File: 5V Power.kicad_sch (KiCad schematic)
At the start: 1 part, among them U3 TPS54540BDDA

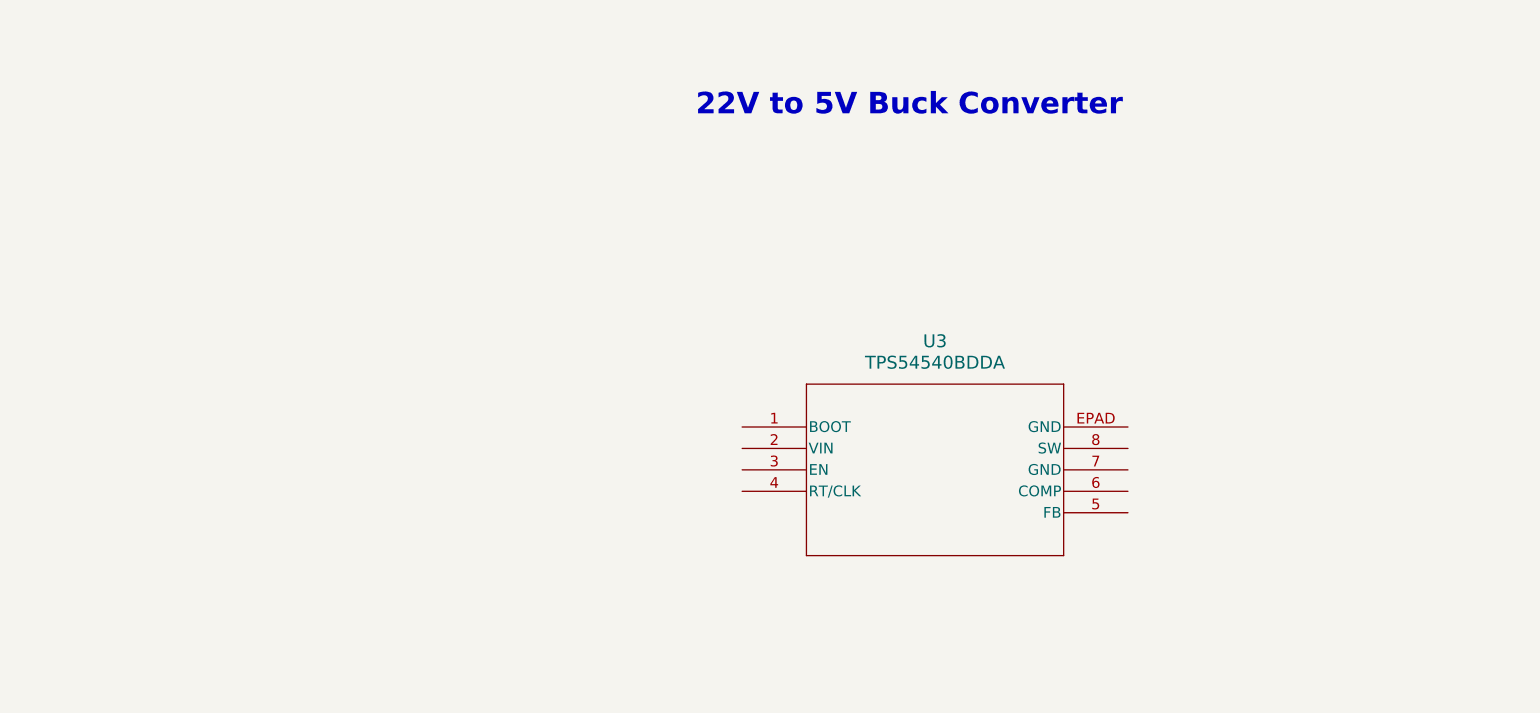
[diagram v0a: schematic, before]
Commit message: Updates to the 5V buck converter
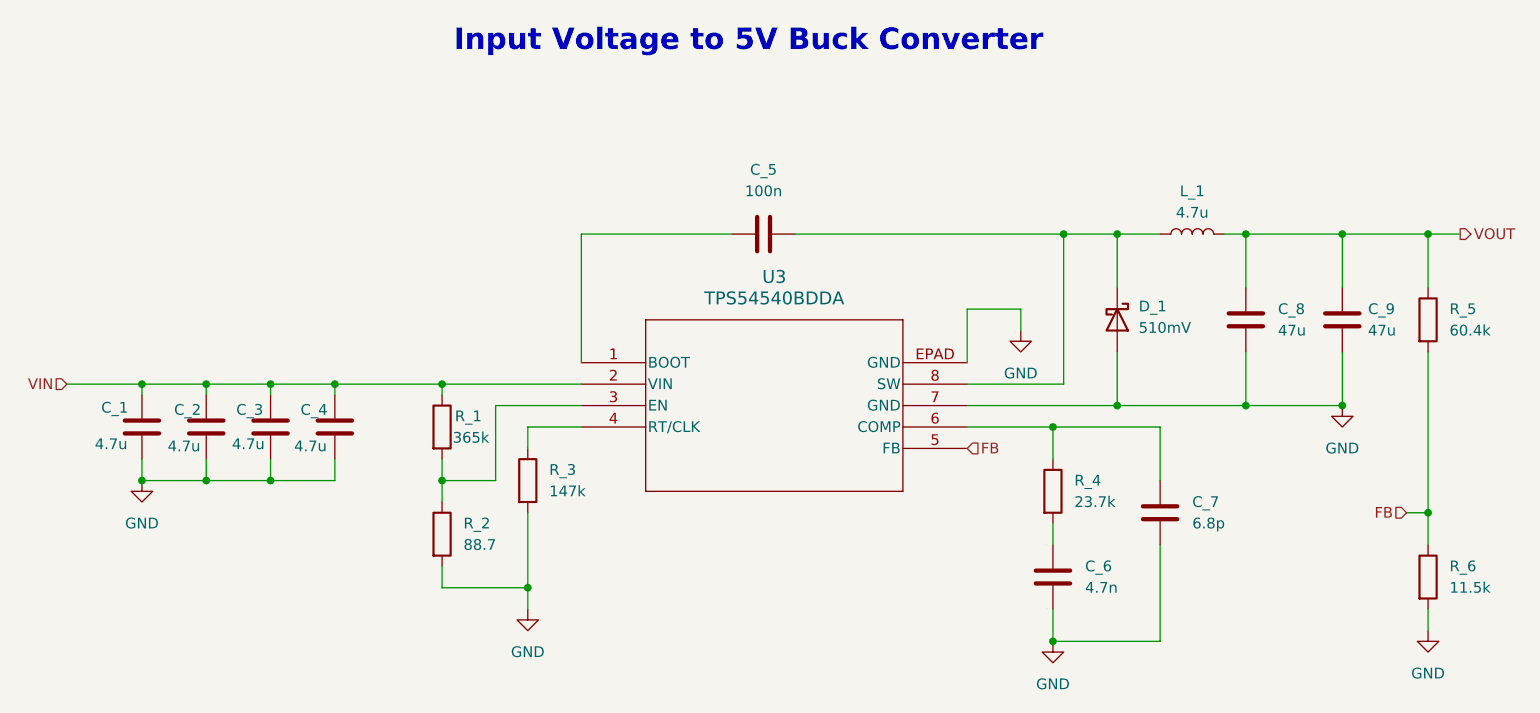
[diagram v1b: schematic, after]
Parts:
- added C_1, C_2, C_3, C_4: 4.7u, symbol Device:C
- added C_5: 100n, symbol Device:C
- added C_6: 4.7n, symbol Device:C
- added C_7: 6.8p, symbol Device:C
- added C_8, C_9: 47u, symbol Device:C
- added D_1: 510mV, symbol Device:D_Schottky
- added L_1: 4.7u, symbol Device:L
- added R_1: 365k, symbol Device:R
- added R_2: 88.7, symbol Device:R
- added R_3: 147k, symbol Device:R
- added R_4: 23.7k, symbol Device:R
- added R_5: 60.4k, symbol Device:R
- added R_6: 11.5k, symbol Device:R
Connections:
- net at U3.1 (BOOT): now also C_5.2
- net VIN: now reaches U3.2 (VIN)
- net VIN: now also C_1.1, C_2.1, C_3.1, C_4.1, R_1.1
- net at U3.3 (EN): now also R_1.2, R_2.1
- net at U3.4 (RT/CLK): now also R_3.1
- net FB: now reaches U3.5 (FB)
- net FB: now also R_5.2, R_6.1
- net at U3.6 (COMP): now also C_7.1, R_4.1
- net GND: now reaches U3.7 (GND)
- net GND: now also U3.EPAD (GND), C_1.2, C_2.2, C_3.2, C_4.2, C_6.2, C_7.2, C_8.2, C_9.2, D_1.2 (A), R_2.2, R_3.2, R_6.2
- net at U3.8 (SW): now also C_5.1, D_1.1 (K), L_1.1
- new net: C_6.1, R_4.2
- new net VOUT: C_8.1, C_9.1, L_1.2, R_5.1
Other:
- note added: "Input Voltage to 5V Buck Converter"
- note removed: "22V to 5V Buck Converter"
- moved on the sheet: U3

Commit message: Added new potentiometer
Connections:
- net VOUT renamed +5V
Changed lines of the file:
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@@
-		)
-	)
-	(hierarchical_label "VOUT"
-		(shape output)
-		(at 203.2 72.39 0)
-		(effects
-			(font
-				(size 1.27 1.27)
-			)
-			(justify left)
 		)
 	)
@@
 		)
 	)
+	(symbol
+		(lib_id "power:+5V")
+		(at 203.2 72.39 0)
+		(unit 1)
+		(body_style 1)
+		(exclude_from_sim no)
+		(in_bom yes)
+		(on_board yes)
+		(in_pos_files yes)
+		(dnp no)
+		(fields_autoplaced yes)
+		(property "Reference" "#PWR022"
+			(at 203.2 76.2 0)
+			(hide yes)
+			(show_name no)
+			(do_not_autoplace no)
+			(effects
+				(font
+					(size 1.27 1.27)
+				)
+			)
+		)
+		(property "Value" "+5V"
+			(at 203.2 67.31 0)
+			(show_name no)
+			(do_not_autoplace no)
+			(effects
+				(font
+					(size 1.27 1.27)
+				)
+			)
+		)
+		(property "Footprint" ""
+			(at 203.2 72.39 0)
+			(hide yes)
+			(show_name no)
+			(do_not_autoplace no)
+			(effects
+				(font
+					(size 1.27 1.27)
+				)
+			)
+		)
+		(property "Datasheet" ""
+			(at 203.2 72.39 0)
+			(hide yes)
+			(show_name no)
+			(do_not_autoplace no)
+			(effects
+				(font
+					(size 1.27 1.27)
+				)
+			)
+		)
+		(property "Description" "Power symbol creates a global label with name \"+5V\""
+			(at 203.2 72.39 0)
+			(hide yes)
+			(show_name no)
+			(do_not_autoplace no)
+			(effects
+				(font
+					(size 1.27 1.27)
+				)
+			)
+		)
+		(pin "1"
+		)
+		(instances
+			(project "LEOS-F26-power"
+				(path "/3703ddf2-8141-438d-86a8-1eaec9672d0d/528ff9b0-a904-4a78-86c6-11cbf84face6"
+					(reference "#PWR022")
+					(unit 1)
+				)
+			)
+		)
+	)

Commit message: added footprints
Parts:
- C_1, C_2, C_3, C_4, C_5, C_6, C_7, C_8, C_9: footprint (none) -> Capacitor_SMD:C_0805_2012Metric
- D_1: footprint (none) -> Diode_SMD:D_0805_2012Metric
- L_1: footprint (none) -> Inductor_SMD:L_0805_2012Metric
- R_1, R_2, R_3, R_4, R_5, R_6: footprint (none) -> Resistor_SMD:R_0805_2012Metric
- U3: footprint SO-POWERPAD8_DDA_TEX -> (none)
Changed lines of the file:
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@@
 			)
 		)
-		(property "Footprint" ""
+		(property "Footprint" "Capacitor_SMD:C_0805_2012Metric"
 			(at 63.1952 99.06 0)
 			(hide yes)
@@
 			)
 		)
-		(property "Footprint" ""
+		(property "Footprint" "Capacitor_SMD:C_0805_2012Metric"
 			(at 47.9552 99.06 0)
 			(hide yes)
@@
 			)
 		)
-		(property "Footprint" ""
+		(property "Footprint" "Capacitor_SMD:C_0805_2012Metric"
 			(at 178.7652 86.36 0)
 			(hide yes)
@@
 			)
 		)
-		(property "Footprint" "SO-POWERPAD8_DDA_TEX"
+		(property "Footprint" ""
 			(at 99.06 87.63 0)
 			(hide yes)
@@
 			)
 		)
-		(property "Footprint" ""
+		(property "Footprint" "Resistor_SMD:R_0805_2012Metric"
 			(at 197.612 82.55 90)
 			(hide yes)
@@
 			)
 		)
-		(property "Footprint" ""
+		(property "Footprint" "Resistor_SMD:R_0805_2012Metric"
 			(at 80.772 95.25 90)
 			(hide yes)
@@
 			)
 		)
-		(property "Footprint" ""
+		(property "Footprint" "Resistor_SMD:R_0805_2012Metric"
 			(at 90.932 101.6 90)
 			(hide yes)
@@
 			)
 		)
-		(property "Footprint" ""
+		(property "Footprint" "Inductor_SMD:L_0805_2012Metric"
 			(at 171.45 72.39 0)
 			(hide yes)
@@
 			)
 		)
-		(property "Footprint" ""
+		(property "Footprint" "Capacitor_SMD:C_0805_2012Metric"
 			(at 190.1952 86.36 0)
 			(hide yes)
@@
 			)
 		)
-		(property "Footprint" ""
+		(property "Footprint" "Capacitor_SMD:C_0805_2012Metric"
 			(at 55.5752 99.06 0)
 			(hide yes)
@@
 			)
 		)
-		(property "Footprint" ""
+		(property "Footprint" "Capacitor_SMD:C_0805_2012Metric"
 			(at 70.8152 99.06 0)
 			(hide yes)
@@
 			)
 		)
-		(property "Footprint" ""
+		(property "Footprint" "Resistor_SMD:R_0805_2012Metric"
 			(at 80.772 107.95 90)
 			(hide yes)
@@
 			)
 		)
-		(property "Footprint" ""
+		(property "Footprint" "Capacitor_SMD:C_0805_2012Metric"
 			(at 168.6052 109.22 0)
 			(hide yes)
@@
 			)
 		)
-		(property "Footprint" ""
+		(property "Footprint" "Resistor_SMD:R_0805_2012Metric"
 			(at 153.162 102.87 90)
 			(hide yes)
@@
 			)
 		)
-		(property "Footprint" ""
+		(property "Footprint" "Resistor_SMD:R_0805_2012Metric"
 			(at 197.612 113.03 90)
 			(hide yes)
@@
 			)
 		)
-		(property "Footprint" ""
+		(property "Footprint" "Diode_SMD:D_0805_2012Metric"
 			(at 162.56 82.55 0)
 			(hide yes)
@@
 			)
 		)
-		(property "Footprint" ""
+		(property "Footprint" "Capacitor_SMD:C_0805_2012Metric"
 			(at 155.9052 116.84 0)
 			(hide yes)
@@
 			)
 		)
-		(property "Footprint" ""
+		(property "Footprint" "Capacitor_SMD:C_0805_2012Metric"
 			(at 116.84 73.3552 0)
 			(hide yes)

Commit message: testing
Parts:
- C_1, C_2, C_3, C_4: Digikey (none) -> 1276-2970-1-ND; MPN (none) -> CL21B475KOFNFNE; Manufacturer (none) -> Samsung Electro-Mechanics
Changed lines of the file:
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@@
+			)
+		)
+		(property "Digikey" "1276-2970-1-ND"
+			(at 62.23 95.25 0)
+			(hide yes)
+			(show_name no)
+			(do_not_autoplace no)
+			(effects
+				(font
+					(size 1.27 1.27)
+				)
+			)
+		)
+		(property "MPN" "CL21B475KOFNFNE"
+			(at 62.23 95.25 0)
+			(hide yes)
+			(show_name no)
+			(do_not_autoplace no)
+			(effects
+				(font
+					(size 1.27 1.27)
+				)
+			)
+		)
+		(property "Manufacturer" "Samsung Electro-Mechanics"
+			(at 62.23 95.25 0)
+			(hide yes)
+			(show_name no)
+			(do_not_autoplace no)
+			(effects
+				(font
+					(size 1.27 1.27)
+				)
 			)
 		)
@@
 		)
 		(property "Description" "Unpolarized capacitor"
+			(at 46.99 95.25 0)
+			(hide yes)
+			(show_name no)
+			(do_not_autoplace no)
+			(effects
+				(font
+					(size 1.27 1.27)
+				)
+			)
+		)
+		(property "Digikey" "1276-2970-1-ND"
+			(at 46.99 95.25 0)
+			(hide yes)
+			(show_name no)
+			(do_not_autoplace no)
+			(effects
+				(font
+					(size 1.27 1.27)
+				)
+			)
+		)
+		(property "MPN" "CL21B475KOFNFNE"
+			(at 46.99 95.25 0)
+			(hide yes)
+			(show_name no)
+			(do_not_autoplace no)
+			(effects
+				(font
+					(size 1.27 1.27)
+				)
+			)
+		)
+		(property "Manufacturer" "Samsung Electro-Mechanics"
 			(at 46.99 95.25 0)
 			(hide yes)
@@
 			)
 		)
+		(property "Digikey" "1276-2970-1-ND"
+			(at 54.61 95.25 0)
+			(hide yes)
+			(show_name no)
+			(do_not_autoplace no)
+			(effects
+				(font
+					(size 1.27 1.27)
+				)
+			)
+		)
+		(property "MPN" "CL21B475KOFNFNE"
+			(at 54.61 95.25 0)
+			(hide yes)
+			(show_name no)
+			(do_not_autoplace no)
+			(effects
+				(font
+					(size 1.27 1.27)
+				)
+			)
+		)
+		(property "Manufacturer" "Samsung Electro-Mechanics"
+			(at 54.61 95.25 0)
+			(hide yes)
+			(show_name no)
+			(do_not_autoplace no)
+			(effects
+				(font
+					(size 1.27 1.27)
+				)
+			)
+		)
 		(pin "2"
 		)
@@
 			(at 69.85 95.25 0)
 			(hide yes)
+			(show_name no)
+			(do_not_autoplace no)
+			(effects
+				(font
+					(size 1.27 1.27)
+				)
+			)
+		)
+		(property "Digikey" "1276-2970-1-ND"
+			(at 69.85 95.25 0)
+			(hide yes)
+			(show_name no)
+			(do_not_autoplace no)
+			(effects
+				(font
+					(size 1.27 1.27)
+				)
+			)
+		)
+		(property "MPN" "CL21B475KOFNFNE"
+			(at 69.85 95.25 0)
+			(hide yes)
+			(show_name no)
+			(do_not_autoplace no)
+			(effects
+				(font
+					(size 1.27 1.27)
+				)
+			)
+		)
+		(property "Manufacturer" "Samsung Electro-Mechanics"
+			(at 69.85 95.25 0)
+			(hide yes)

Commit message: capacitor
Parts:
- C_6: Digikey (none) -> 399-C0805C472J3GEC7210CT-ND; MPN (none) -> C0805C472J3GEC7210; Manufacturer (none) -> KEMET
- C_7: Digikey (none) -> 399-C0805C689C3HACAUTOCT-ND; MPN (none) -> C0805C689C3HACAUTO; Manufacturer (none) -> KEMET
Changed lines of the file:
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@@
+			)
+		)
+		(property "Digikey" "399-C0805C689C3HACAUTOCT-ND"
+			(at 167.64 105.41 0)
+			(hide yes)
+			(show_name no)
+			(do_not_autoplace no)
+			(effects
+				(font
+					(size 1.27 1.27)
+				)
+			)
+		)
+		(property "MPN" "C0805C689C3HACAUTO"
+			(at 167.64 105.41 0)
+			(hide yes)
+			(show_name no)
+			(do_not_autoplace no)
+			(effects
+				(font
+					(size 1.27 1.27)
+				)
+			)
+		)
+		(property "Manufacturer" "KEMET"
+			(at 167.64 105.41 0)
+			(hide yes)
+			(show_name no)
+			(do_not_autoplace no)
+			(effects
+				(font
+					(size 1.27 1.27)
+				)
 			)
 		)
@@
 			(at 154.94 113.03 0)
 			(hide yes)
+			(show_name no)
+			(do_not_autoplace no)
+			(effects
+				(font
+					(size 1.27 1.27)
+				)
+			)
+		)
+		(property "Digikey" "399-C0805C472J3GEC7210CT-ND"
+			(at 154.94 113.03 0)
+			(hide yes)
+			(show_name no)
+			(do_not_autoplace no)
+			(effects
+				(font
+					(size 1.27 1.27)
+				)
+			)
+		)
+		(property "MPN" "C0805C472J3GEC7210"
+			(at 154.94 113.03 0)
+			(hide yes)
+			(show_name no)
+			(do_not_autoplace no)
+			(effects
+				(font
+					(size 1.27 1.27)
+				)
+			)
+		)
+		(property "Manufacturer" "KEMET"
+			(at 154.94 113.03 0)
+			(hide yes)

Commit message: resistor values
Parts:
- R_1: Digikey (none) -> RMCF0805FT365KCT-ND; MPN (none) -> RMCF0805FT365K; Manufacturer (none) -> Stackpole Electronics Inc
- R_2: Digikey (none) -> 738-RMCF0805FT88R7CT-ND; MPN (none) -> RMCF0805FT88R7; Manufacturer (none) -> Stackpole Electronics Inc
- R_3: Digikey (none) -> RMCF0805FT147KCT-ND; MPN (none) -> RMCF0805FT147K; Manufacturer (none) -> Stackpole Electronics Inc
- R_4: Digikey (none) -> 738-RMCF0805FT23K7CT-ND; MPN (none) -> RMCF0805FT23K7; Manufacturer (none) -> Stackpole Electronics Inc
- R_5: Digikey (none) -> RMCF0805FT60K4CT-ND; MPN (none) -> RMCF0805FT60K4; Manufacturer (none) -> Stackpole Electronics Inc
- R_6: Digikey (none) -> RMCF0805FT11K5CT-ND; MPN (none) -> RMCF0805FT11K5; Manufacturer (none) -> Stackpole Electronics Inc
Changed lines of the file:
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@@
+			)
+		)
+		(property "Digikey" "RMCF0805FT60K4CT-ND"
+			(at 199.39 82.55 0)
+			(hide yes)
+			(show_name no)
+			(do_not_autoplace no)
+			(effects
+				(font
+					(size 1.27 1.27)
+				)
+			)
+		)
+		(property "MPN" "RMCF0805FT60K4"
+			(at 199.39 82.55 0)
+			(hide yes)
+			(show_name no)
+			(do_not_autoplace no)
+			(effects
+				(font
+					(size 1.27 1.27)
+				)
+			)
+		)
+		(property "Manufacturer" "Stackpole Electronics Inc"
+			(at 199.39 82.55 0)
+			(hide yes)
+			(show_name no)
+			(do_not_autoplace no)
+			(effects
+				(font
+					(size 1.27 1.27)
+				)
 			)
 		)
@@
 		)
 		(property "Description" "Resistor"
+			(at 82.55 95.25 0)
+			(hide yes)
+			(show_name no)
+			(do_not_autoplace no)
+			(effects
+				(font
+					(size 1.27 1.27)
+				)
+			)
+		)
+		(property "Digikey" "RMCF0805FT365KCT-ND"
+			(at 82.55 95.25 0)
+			(hide yes)
+			(show_name no)
+			(do_not_autoplace no)
+			(effects
+				(font
+					(size 1.27 1.27)
+				)
+			)
+		)
+		(property "MPN" "RMCF0805FT365K"
+			(at 82.55 95.25 0)
+			(hide yes)
+			(show_name no)
+			(do_not_autoplace no)
+			(effects
+				(font
+					(size 1.27 1.27)
+				)
+			)
+		)
+		(property "Manufacturer" "Stackpole Electronics Inc"
 			(at 82.55 95.25 0)
 			(hide yes)
@@
 			)
 		)
+		(property "Digikey" "RMCF0805FT147KCT-ND"
+			(at 92.71 101.6 0)
+			(hide yes)
+			(show_name no)
+			(do_not_autoplace no)
+			(effects
+				(font
+					(size 1.27 1.27)
+				)
+			)
+		)
+		(property "MPN" "RMCF0805FT147K"
+			(at 92.71 101.6 0)
+			(hide yes)
+			(show_name no)
+			(do_not_autoplace no)
+			(effects
+				(font
+					(size 1.27 1.27)
+				)
+			)
+		)
+		(property "Manufacturer" "Stackpole Electronics Inc"
+			(at 92.71 101.6 0)
+			(hide yes)
+			(show_name no)
+			(do_not_autoplace no)
+			(effects
+				(font
+					(size 1.27 1.27)
+				)
+			)
+		)
 		(pin "1"
 		)
@@
 			)
 		)
+		(property "Digikey" "738-RMCF0805FT88R7CT-ND"
+			(at 82.55 107.95 0)
+			(hide yes)
+			(show_name no)
+			(do_not_autoplace no)
+			(effects
+				(font
+					(size 1.27 1.27)
+				)
+			)
+		)
+		(property "MPN" "RMCF0805FT88R7"
+			(at 82.55 107.95 0)
+			(hide yes)
+			(show_name no)
+			(do_not_autoplace no)
+			(effects
+				(font
+					(size 1.27 1.27)
+				)
+			)
+		)
+		(property "Manufacturer" "Stackpole Electronics Inc"
+			(at 82.55 107.95 0)
+			(hide yes)
+			(show_name no)
+			(do_not_autoplace no)
+			(effects
+				(font
+					(size 1.27 1.27)
+				)
+			)
+		)
 		(pin "2"
 		)
@@
 			)
 		)
+		(property "Digikey" "738-RMCF0805FT23K7CT-ND"
+			(at 154.94 102.87 0)
+			(hide yes)
+			(show_name no)
+			(do_not_autoplace no)
+			(effects
+				(font
+					(size 1.27 1.27)
+				)
+			)
+		)
+		(property "MPN" "RMCF0805FT23K7"
+			(at 154.94 102.87 0)
+			(hide yes)
+			(show_name no)
+			(do_not_autoplace no)
+			(effects
+				(font
+					(size 1.27 1.27)
+				)
+			)
+		)
+		(property "Manufacturer" "Stackpole Electronics Inc"
+			(at 154.94 102.87 0)
+			(hide yes)
+			(show_name no)
+			(do_not_autoplace no)
+			(effects
+				(font
+					(size 1.27 1.27)
+				)
+			)
+		)
 		(pin "1"
 		)
@@
 			(at 199.39 113.03 0)
 			(hide yes)
+			(show_name no)
+			(do_not_autoplace no)
+			(effects
+				(font
+					(size 1.27 1.27)
+				)
+			)
+		)
+		(property "Digikey" "RMCF0805FT11K5CT-ND"
+			(at 199.39 113.03 0)
+			(hide yes)
+			(show_name no)
+			(do_not_autoplace no)
+			(effects
+				(font
+					(size 1.27 1.27)
+				)
+			)
+		)
+		(property "MPN" "RMCF0805FT11K5"
+			(at 199.39 113.03 0)
+			(hide yes)
+			(show_name no)
+			(do_not_autoplace no)
+			(effects
+				(font
+					(size 1.27 1.27)
+				)
+			)
+		)
+		(property "Manufacturer" "Stackpole Electronics Inc"
+			(at 199.39 113.03 0)
+			(hide yes)
